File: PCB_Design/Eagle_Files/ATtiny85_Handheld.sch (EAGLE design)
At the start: 21 parts

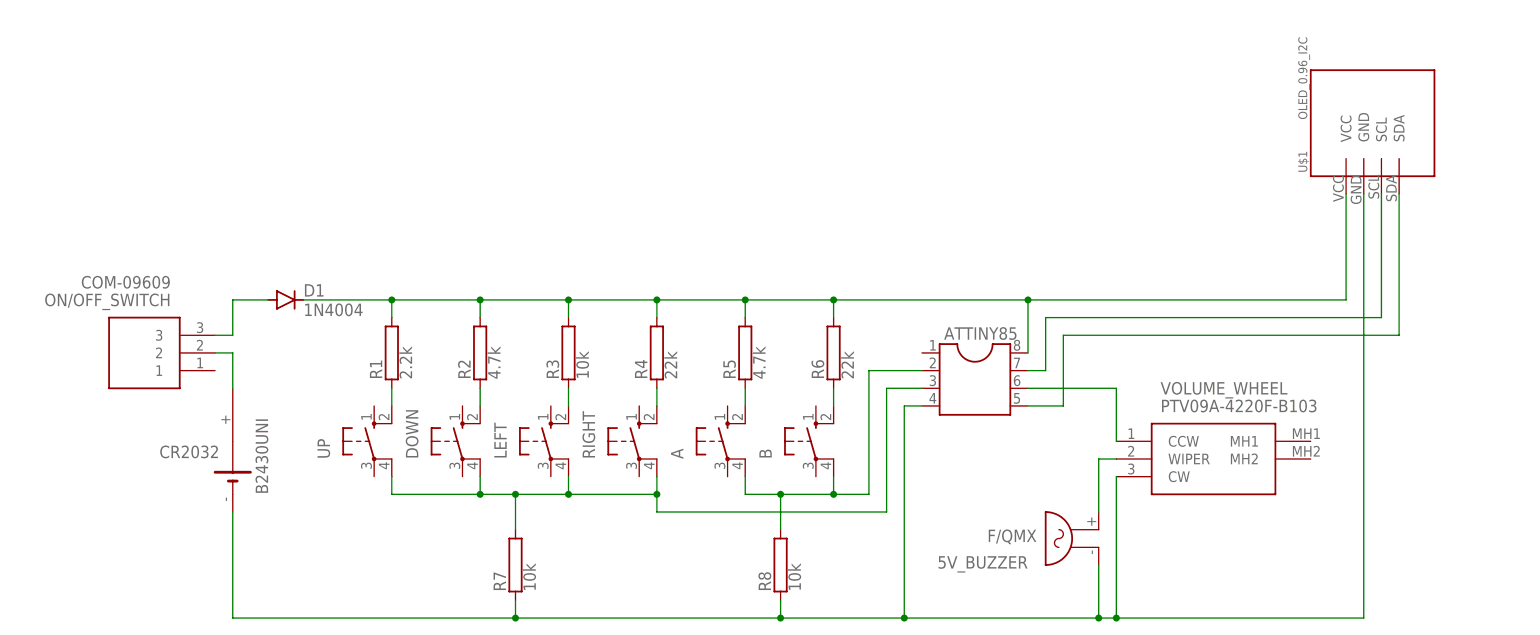
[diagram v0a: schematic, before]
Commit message: V1.2.0 Updated the PCB to V1.1
- Option of using silicone or tactile buttons
- Removed D1
- Hand-router, thicker traces
- Broke the schematic into sections to make it easier to follow
- Update/fixed the battery holder footprint
- Changed the switch footprint to use an angled slide switch
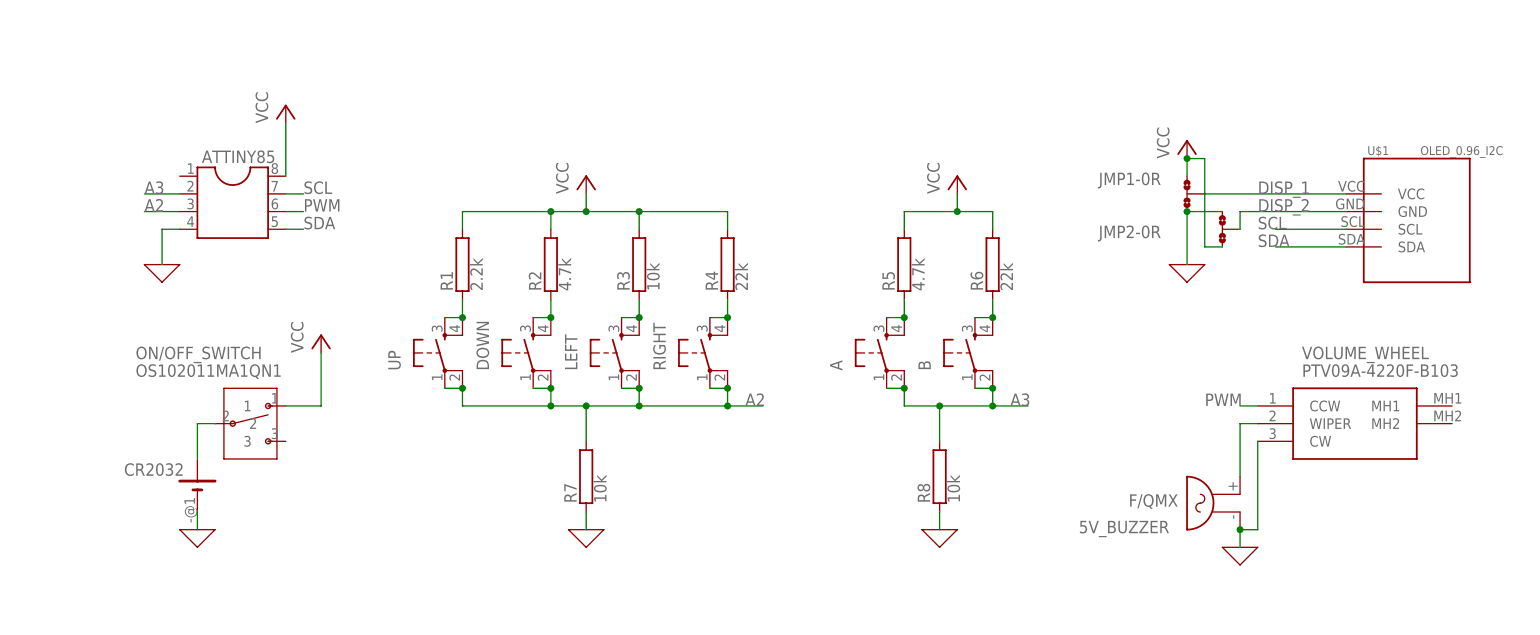
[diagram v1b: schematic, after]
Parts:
- removed D1: 1N4004, diode:1N4004
- added JMP1, JMP2: 0R-JUMPA, jump-0r-smd:0R-JUMPA
- A, B, DOWN, LEFT, RIGHT, UP: value (none) -> TACTILE/SILICONE_BUTTON; device switch-omron:10-XX -> Tactile_&_SIlicone_Button:TACTILE/SILICONE_BUTTON
- CR2032: value B2430UNI -> CR2032_BATTERY_HOLDER; device battery:B2430UNI -> CR2032_Battery_Holder:CR2032_BATTERY_HOLDER
- ON/OFF_SWITCH: value COM-09609 -> OS102011MA1QN1; device COM-09609:COM-09609 -> OS102011MA1QN1:OS102011MA1QN1
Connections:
- net N$12 renamed SDA
- net N$13 renamed SCL
- net N$15 renamed PWM
- removed net N$10: A.P1, ATTINY85.2, B.P1, R8.2
- removed net N$11: 5V_BUZZER.1, ATTINY85.4, CR2032.-, R7.1, R8.1, U$1.GND, VOLUME_WHEEL.CW
- removed net N$16: D1.A, ON/OFF_SWITCH.3
- removed net N$2: ATTINY85.8, D1.C, R1.2, R2.2, R3.2, R4.2, R5.2, R6.2, U$1.VCC
- removed net N$7: ATTINY85.3, DOWN.P1, LEFT.P1, R7.2, RIGHT.P1, UP.P1
- new net A2: ATTINY85.3, DOWN.P, DOWN.P1, LEFT.P, LEFT.P1, R7.2, RIGHT.P, RIGHT.P1, UP.P, UP.P1
- new net A3: A.P, A.P1, ATTINY85.2, B.P, B.P1, R8.2
- new net DISP_1: JMP1-0R.2, U$1.VCC
- new net DISP_2: JMP2-0R.2, U$1.GND
- new net GND: 5V_BUZZER.1, ATTINY85.4, CR2032.-, JMP1-0R.3, JMP2-0R.1, R7.1, R8.1, VOLUME_WHEEL.CW
- new net VCC: ATTINY85.8, JMP1-0R.1, JMP2-0R.3, ON/OFF_SWITCH.1, R1.2, R2.2, R3.2, R4.2, R5.2, R6.2
- net N$1: now also CR2032.+@1; no longer CR2032.+
- net N$3: now also RIGHT.S
- net N$4: now also LEFT.S
- net N$5: now also DOWN.S
- net N$6: now also UP.S
- net N$8: now also A.S
- net N$9: now also B.S
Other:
- moved on the sheet: 5V_BUZZER, ATTINY85, R1, R2, R3, R4, R5, R6, R7, R8, U$1, VOLUME_WHEEL
